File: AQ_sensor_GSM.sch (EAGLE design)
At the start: 49 parts, among them IC2 MCP73831/OT, J1 F-1X03-SIP-100-32, SW1 PCM12SMTR, SW2 PCM12SMTR, U2 TEXAS_INSTRUMENTS_SN74HC125TE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, U3 TEXAS_INSTRUMENTS_LM1117IMP-3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, X1 53048-08, X2 SIMLOCK-C707_10M006_512_2, X4 50 Ohms

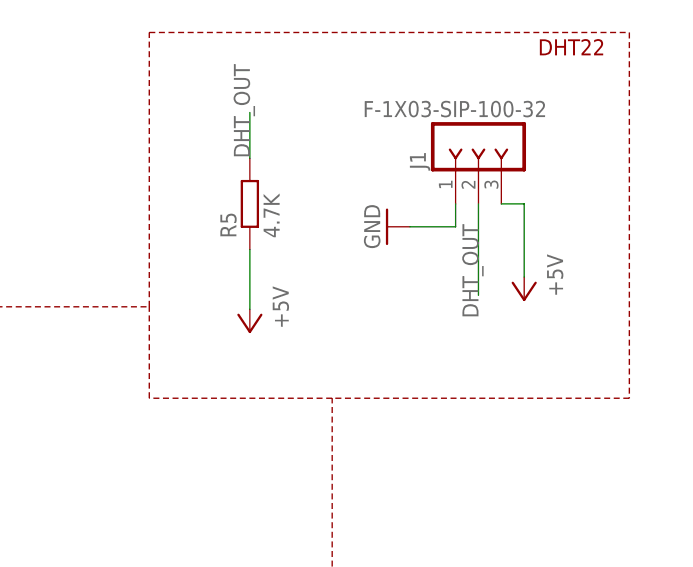
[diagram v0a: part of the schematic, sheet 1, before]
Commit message: Added stitching vias
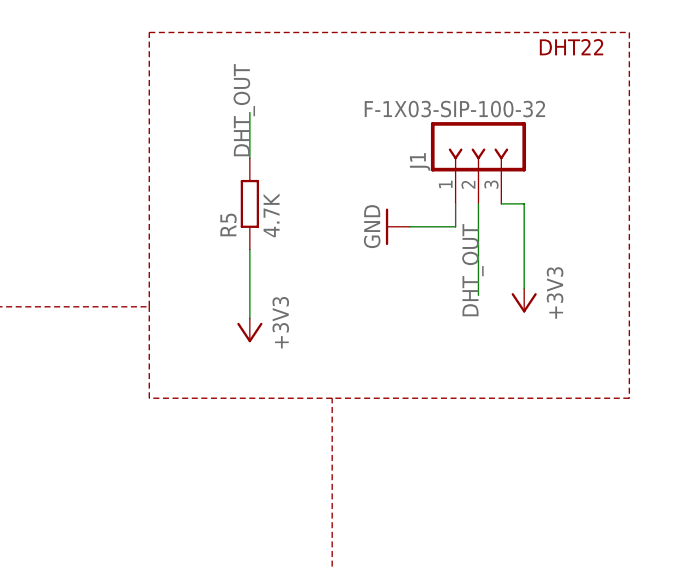
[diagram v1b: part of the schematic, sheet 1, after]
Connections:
- net +3V3: now also J1.3, R5.1
- net +5V: no longer J1.3, R5.1
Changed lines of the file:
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@@
 <setting verticaltext="up"/>
 </settings>
-<grid distance="0.1" unitdist="inch" unit="inch" style="lines" multiple="1" display="no" altdistance="0.01" altunitdist="inch" altunit="inch"/>
+<grid distance="0.01" unitdist="inch" unit="inch" style="dots" multiple="1" display="yes" altdistance="0.01" altunitdist="inch" altunit="inch"/>
 <layers>
 <layer number="1" name="Top" color="4" fill="1" visible="no" active="no"/>
@@
 <part name="H4" library="AQ_sensor_GSM" library_urn="urn:adsk.eagle:library:30300195" deviceset="MOUNT-PAD-ROUND" device="2.8" package3d_urn="urn:adsk.eagle:package:30300289/1"/>
 <part name="GND61" library="supply1" library_urn="urn:adsk.eagle:library:371" deviceset="GND" device=""/>
-<part name="P+12" library="supply1" library_urn="urn:adsk.eagle:library:371" deviceset="+5V" device=""/>
-<part name="P+13" library="supply1" library_urn="urn:adsk.eagle:library:371" deviceset="+5V" device=""/>
 <part name="GND13" library="supply1" library_urn="urn:adsk.eagle:library:371" deviceset="GND" device=""/>
 <part name="DHT" library="led" library_urn="urn:adsk.eagle:library:259" deviceset="LED" device="CHIP-LED0603" package3d_urn="urn:adsk.eagle:package:15819/3" value="GREEN"/>
@@
 <part name="P+8" library="supply1" library_urn="urn:adsk.eagle:library:371" deviceset="+5V" device=""/>
 <part name="GND8" library="supply1" library_urn="urn:adsk.eagle:library:371" deviceset="GND" device=""/>
+<part name="+3V1" library="supply1" library_urn="urn:adsk.eagle:library:371" deviceset="+3V3" device=""/>
+<part name="+3V2" library="supply1" library_urn="urn:adsk.eagle:library:371" deviceset="+3V3" device=""/>
 </parts>
 <sheets>
@@
 <attribute name="VALUE" x="202.184" y="16.51" size="1.778" layer="96"/>
 </instance>
-<instance part="P+12" gate="1" x="364.236" y="155.702" smashed="yes" rot="R180">
-<attribute name="VALUE" x="366.776" y="160.782" size="1.778" layer="96" rot="R270"/>
-</instance>
-<instance part="P+13" gate="1" x="333.756" y="152.146" smashed="yes" rot="R180">
-<attribute name="VALUE" x="336.296" y="157.226" size="1.778" layer="96" rot="R270"/>
-</instance>
 <instance part="GND13" gate="1" x="136.398" y="237.998" smashed="yes" rot="R270">
 <attribute name="VALUE" x="133.858" y="240.538" size="1.778" layer="96" rot="R270"/>
@@
 <instance part="GND8" gate="1" x="96.52" y="201.93" smashed="yes">
 <attribute name="VALUE" x="93.98" y="199.39" size="1.778" layer="96"/>
+</instance>
+<instance part="+3V1" gate="G$1" x="333.756" y="151.13" smashed="yes" rot="R180">
+<attribute name="VALUE" x="336.296" y="156.21" size="1.778" layer="96" rot="R270"/>
+</instance>
+<instance part="+3V2" gate="G$1" x="364.236" y="154.432" smashed="yes" rot="R180">
+<attribute name="VALUE" x="366.776" y="159.512" size="1.778" layer="96" rot="R270"/>
 </instance>
 </instances>
@@
 <junction x="55.88" y="22.86"/>
 </segment>
-<segment>
-<pinref part="J1" gate="G$1" pin="3"/>
-<wire x1="361.696" y1="166.37" x2="364.236" y2="166.37" width="0.1524" layer="91"/>
-<wire x1="364.236" y1="166.37" x2="364.236" y2="158.242" width="0.1524" layer="91"/>
-<pinref part="P+12" gate="1" pin="+5V"/>
-</segment>
-<segment>
-<pinref part="R5" gate="G$1" pin="1"/>
-<wire x1="333.756" y1="161.29" x2="333.756" y2="154.686" width="0.1524" layer="91"/>
-<pinref part="P+13" gate="1" pin="+5V"/>
-</segment>
 </net>
 <net name="+3V3" class="1">
@@
 <junction x="93.98" y="25.4"/>
 </segment>
+<segment>
+<pinref part="J1" gate="G$1" pin="3"/>
+<wire x1="361.696" y1="166.37" x2="364.236" y2="166.37" width="0.1524" layer="91"/>
+<wire x1="364.236" y1="166.37" x2="364.236" y2="156.972" width="0.1524" layer="91"/>
+<pinref part="+3V2" gate="G$1" pin="+3V3"/>
+</segment>
+<segment>
+<pinref part="R5" gate="G$1" pin="1"/>
+<wire x1="333.756" y1="161.29" x2="333.756" y2="153.67" width="0.1524" layer="91"/>
+<pinref part="+3V1" gate="G$1" pin="+3V3"/>
+</segment>
 </net>
